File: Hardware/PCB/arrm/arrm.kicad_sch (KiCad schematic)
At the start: 9 parts, among them J1 3_pin_Molex_header, J2 3_pin_Molex_connector, J3 2_pin_Molex_header, J4 2_pin_Molex_connector, J5 2_pin_Molex_header, J6 2_pin_Molex_connector

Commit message: Rename project, cleanup
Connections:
- net Main PCB/CARRLVL_CW renamed Main PCB/CARRLVL_WIP
- net Main PCB/SIGLVL_CW renamed Main PCB/SIGLVL_WIP
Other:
- sheet Main PCB ports: added CARRLVL_WIP, SIGLVL_WIP; removed CARRLVL_CW, SIGLVL_CW
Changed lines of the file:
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@@
       (effects (font (size 1.27 1.27)) (justify right))
     )
-    (pin "SIGLVL_CW" output (at 113.03 106.68 0)
+    (pin "SIGLVL_WIP" output (at 113.03 106.68 0)
       (effects (font (size 1.27 1.27)) (justify right))
     )
@@
       (effects (font (size 1.27 1.27)) (justify right))
     )
-    (pin "CARRLVL_CW" output (at 113.03 97.79 0)
+    (pin "CARRLVL_WIP" output (at 113.03 97.79 0)
       (effects (font (size 1.27 1.27)) (justify right))
     )

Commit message: Final pre fab tweaks, Gerbers
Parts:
- J1: value 3_pin_Molex_header -> (none); footprint ao_tht:Molex_KK-254_AE-6410-03A_1x03_P2.54mm_Vertical -> (none)
- J2: renamed from J3; value 2_pin_Molex_header -> (none); footprint ao_tht:Molex_KK-254_AE-6410-02A_1x02_P2.54mm_Vertical -> (none)
- J3: renamed from J5; value 2_pin_Molex_header -> (none); footprint ao_tht:Molex_KK-254_AE-6410-02A_1x02_P2.54mm_Vertical -> (none)
- J4: renamed from J2; value 3_pin_Molex_connector -> (none)
- J5: renamed from J4; value 2_pin_Molex_connector -> (none)
- J6: value 2_pin_Molex_connector -> (none)
- RV1: value 100k -> (none); footprint ao_tht:Potentiometer_Alpha_16mm_Single_Vertical -> (none)
- RV2: renamed from RV3; value 100k -> (none); footprint ao_tht:Potentiometer_Alpha_16mm_Single_Vertical -> (none)
- RV3: renamed from RV5; value 100k -> (none); footprint ao_tht:Potentiometer_Alpha_16mm_Single_Vertical -> (none)

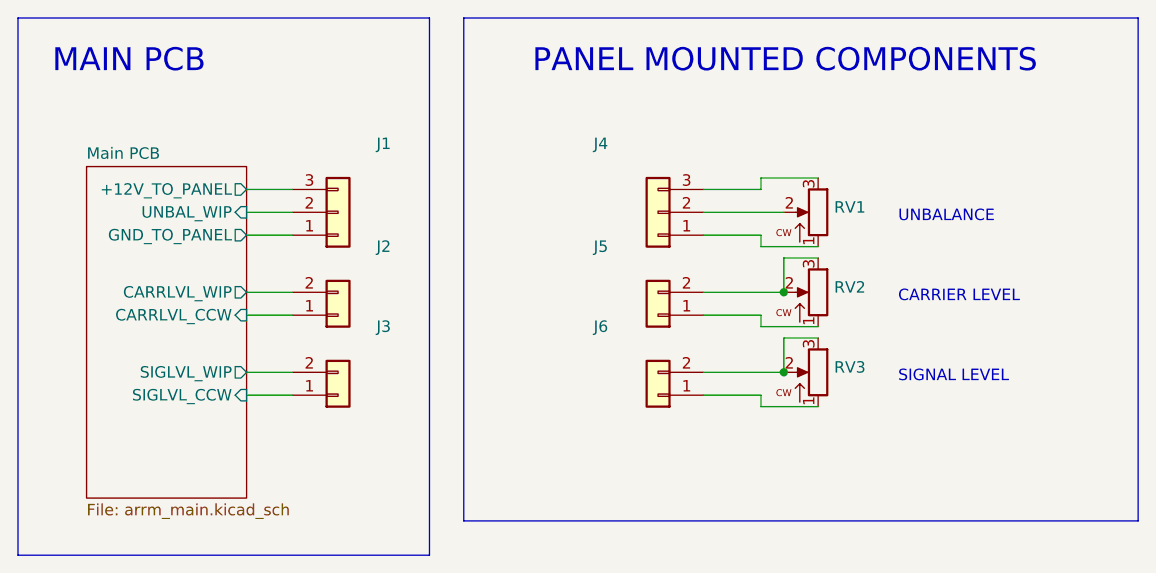
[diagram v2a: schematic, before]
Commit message: Fix footprint path; fix transformer footprint
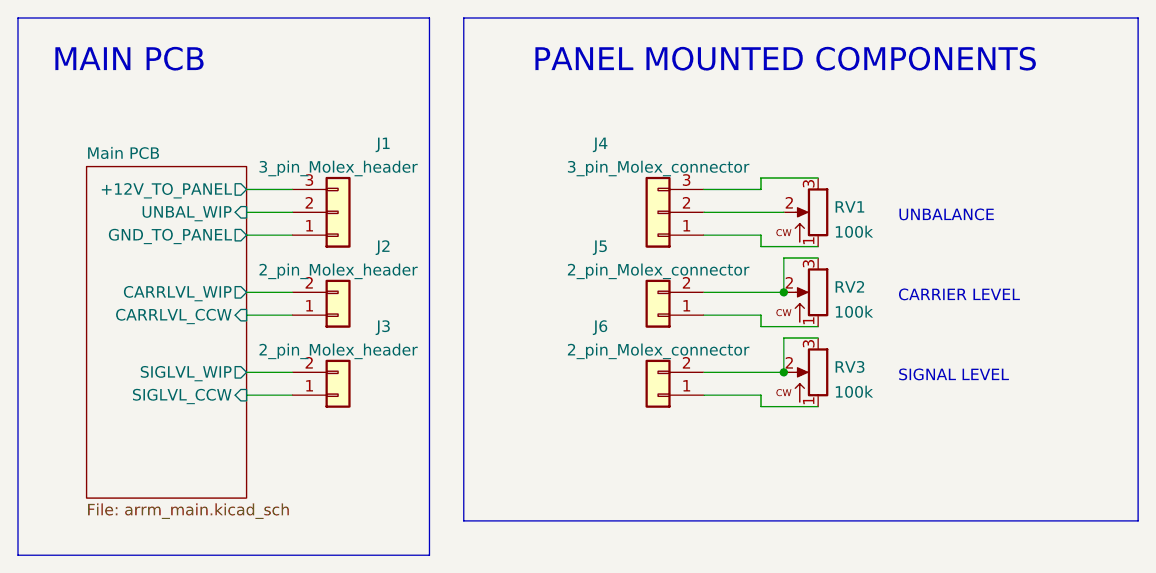
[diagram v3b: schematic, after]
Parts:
- J1: value (none) -> 3_pin_Molex_header; footprint (none) -> ao_tht:Molex_KK-254_AE-6410-03A_1x03_P2.54mm_Vertical
- J2, J3: value (none) -> 2_pin_Molex_header; footprint (none) -> ao_tht:Molex_KK-254_AE-6410-02A_1x02_P2.54mm_Vertical
- J4: value (none) -> 3_pin_Molex_connector
- J5, J6: value (none) -> 2_pin_Molex_connector
- RV1, RV2, RV3: value (none) -> 100k; footprint (none) -> ao_tht:Potentiometer_Alpha_16mm_Single_Vertical
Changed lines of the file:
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@@
       (effects (font (size 1.27 1.27)) (justify right))
     )
-    (property "Value" "" (id 1) (at 178.308 108.9022 0)
+    (property "Value" "100k" (id 1) (at 178.308 108.9022 0)
       (effects (font (size 1.27 1.27)) (justify right))
     )
-    (property "Footprint" "" (id 2) (at 176.53 106.68 0)
+    (property "Footprint" "ao_tht:Potentiometer_Alpha_16mm_Single_Vertical" (id 2) (at 176.53 106.68 0)
       (effects (font (size 1.27 1.27)) hide)
     )
@@
     (in_bom yes) (on_board no)
     (property "Reference" "J4" (id 0) (at 152.4 81.28 0))
-    (property "Value" "" (id 1) (at 158.75 83.8986 0))
+    (property "Value" "3_pin_Molex_connector" (id 1) (at 158.75 83.8986 0))
     (property "Footprint" "" (id 2) (at 158.75 88.9 0)
       (effects (font (size 1.27 1.27)) hide)
@@
       (effects (font (size 1.27 1.27)) (justify right))
     )
-    (property "Value" "" (id 1) (at 178.308 100.0122 0)
+    (property "Value" "100k" (id 1) (at 178.308 100.0122 0)
       (effects (font (size 1.27 1.27)) (justify right))
     )
-    (property "Footprint" "" (id 2) (at 176.53 97.79 0)
+    (property "Footprint" "ao_tht:Potentiometer_Alpha_16mm_Single_Vertical" (id 2) (at 176.53 97.79 0)
       (effects (font (size 1.27 1.27)) hide)
     )
@@
     (in_bom yes) (on_board yes)
     (property "Reference" "J2" (id 0) (at 128.27 92.71 0))
-    (property "Value" "" (id 1) (at 123.19 95.3286 0))
-    (property "Footprint" "" (id 2) (at 123.19 100.33 0)
+    (property "Value" "2_pin_Molex_header" (id 1) (at 123.19 95.3286 0))
+    (property "Footprint" "ao_tht:Molex_KK-254_AE-6410-02A_1x02_P2.54mm_Vertical" (id 2) (at 123.19 100.33 0)
       (effects (font (size 1.27 1.27)) hide)
     )
@@
       (effects (font (size 1.27 1.27)) (justify right))
     )
-    (property "Value" "" (id 1) (at 178.308 91.1222 0)
+    (property "Value" "100k" (id 1) (at 178.308 91.1222 0)
       (effects (font (size 1.27 1.27)) (justify right))
     )
-    (property "Footprint" "" (id 2) (at 176.53 88.9 0)
+    (property "Footprint" "ao_tht:Potentiometer_Alpha_16mm_Single_Vertical" (id 2) (at 176.53 88.9 0)
       (effects (font (size 1.27 1.27)) hide)
     )
@@
     (in_bom yes) (on_board yes)
     (property "Reference" "J1" (id 0) (at 128.27 81.28 0))
-    (property "Value" "" (id 1) (at 123.19 83.8986 0))
-    (property "Footprint" "" (id 2) (at 123.19 88.9 0)
+    (property "Value" "3_pin_Molex_header" (id 1) (at 123.19 83.8986 0))
+    (property "Footprint" "ao_tht:Molex_KK-254_AE-6410-03A_1x03_P2.54mm_Vertical" (id 2) (at 123.19 88.9 0)
       (effects (font (size 1.27 1.27)) hide)
     )
@@
     (in_bom yes) (on_board no)
     (property "Reference" "J6" (id 0) (at 152.4 101.6 0))
-    (property "Value" "" (id 1) (at 158.75 104.2186 0))
+    (property "Value" "2_pin_Molex_connector" (id 1) (at 158.75 104.2186 0))
     (property "Footprint" "" (id 2) (at 158.75 109.22 0)
       (effects (font (size 1.27 1.27)) hide)
@@
     (in_bom yes) (on_board yes)
     (property "Reference" "J3" (id 0) (at 128.27 101.6 0))
-    (property "Value" "" (id 1) (at 123.19 104.2186 0))
-    (property "Footprint" "" (id 2) (at 123.19 109.22 0)
+    (property "Value" "2_pin_Molex_header" (id 1) (at 123.19 104.2186 0))
+    (property "Footprint" "ao_tht:Molex_KK-254_AE-6410-02A_1x02_P2.54mm_Vertical" (id 2) (at 123.19 109.22 0)
       (effects (font (size 1.27 1.27)) hide)
     )
@@
     (in_bom yes) (on_board no)
     (property "Reference" "J5" (id 0) (at 152.4 92.71 0))
-    (property "Value" "" (id 1) (at 158.75 95.3286 0))
+    (property "Value" "2_pin_Molex_connector" (id 1) (at 158.75 95.3286 0))
     (property "Footprint" "" (id 2) (at 158.75 100.33 0)
       (effects (font (size 1.27 1.27)) hide)

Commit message: Post fab updates
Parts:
- J1: value 3_pin_Molex_header -> (none); footprint ao_tht:Molex_KK-254_AE-6410-03A_1x03_P2.54mm_Vertical -> (none)
- J2, J3: value 2_pin_Molex_header -> (none); footprint ao_tht:Molex_KK-254_AE-6410-02A_1x02_P2.54mm_Vertical -> (none)
- J4: value 3_pin_Molex_connector -> (none)
- J5, J6: value 2_pin_Molex_connector -> (none)
- RV1, RV2, RV3: value 100k -> (none); footprint ao_tht:Potentiometer_Alpha_16mm_Single_Vertical -> (none)
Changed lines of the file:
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@@
       (effects (font (size 1.27 1.27)) (justify right))
     )
-    (property "Value" "100k" (id 1) (at 178.308 108.9022 0)
+    (property "Value" "" (id 1) (at 178.308 108.9022 0)
       (effects (font (size 1.27 1.27)) (justify right))
     )
-    (property "Footprint" "ao_tht:Potentiometer_Alpha_16mm_Single_Vertical" (id 2) (at 176.53 106.68 0)
+    (property "Footprint" "" (id 2) (at 176.53 106.68 0)
       (effects (font (size 1.27 1.27)) hide)
     )
@@
     )
     (property "Vendor" "Tayda" (id 4) (at 176.53 106.68 0)
+      (effects (font (size 1.27 1.27)) hide)
+    )
+    (property "Description" "Linear potentiometer, panel mount" (id 5) (at 176.53 106.68 0)
       (effects (font (size 1.27 1.27)) hide)
     )
@@
     (in_bom yes) (on_board no)
     (property "Reference" "J4" (id 0) (at 152.4 81.28 0))
-    (property "Value" "3_pin_Molex_connector" (id 1) (at 158.75 83.8986 0))
+    (property "Value" "" (id 1) (at 158.75 83.8986 0))
     (property "Footprint" "" (id 2) (at 158.75 88.9 0)
       (effects (font (size 1.27 1.27)) hide)
@@
       (effects (font (size 1.27 1.27)) (justify right))
     )
-    (property "Value" "100k" (id 1) (at 178.308 100.0122 0)
+    (property "Value" "" (id 1) (at 178.308 100.0122 0)
       (effects (font (size 1.27 1.27)) (justify right))
     )
-    (property "Footprint" "ao_tht:Potentiometer_Alpha_16mm_Single_Vertical" (id 2) (at 176.53 97.79 0)
+    (property "Footprint" "" (id 2) (at 176.53 97.79 0)
       (effects (font (size 1.27 1.27)) hide)
     )
@@
     )
     (property "Vendor" "Tayda" (id 4) (at 176.53 97.79 0)
+      (effects (font (size 1.27 1.27)) hide)
+    )
+    (property "Description" "Linear potentiometer, panel mount" (id 5) (at 176.53 97.79 0)
       (effects (font (size 1.27 1.27)) hide)
     )
@@
     (in_bom yes) (on_board yes)
     (property "Reference" "J2" (id 0) (at 128.27 92.71 0))
-    (property "Value" "2_pin_Molex_header" (id 1) (at 123.19 95.3286 0))
-    (property "Footprint" "ao_tht:Molex_KK-254_AE-6410-02A_1x02_P2.54mm_Vertical" (id 2) (at 123.19 100.33 0)
+    (property "Value" "" (id 1) (at 123.19 95.3286 0))
+    (property "Footprint" "" (id 2) (at 123.19 100.33 0)
       (effects (font (size 1.27 1.27)) hide)
     )
@@
       (effects (font (size 1.27 1.27)) (justify right))
     )
-    (property "Value" "100k" (id 1) (at 178.308 91.1222 0)
+    (property "Value" "" (id 1) (at 178.308 91.1222 0)
       (effects (font (size 1.27 1.27)) (justify right))
     )
-    (property "Footprint" "ao_tht:Potentiometer_Alpha_16mm_Single_Vertical" (id 2) (at 176.53 88.9 0)
+    (property "Footprint" "" (id 2) (at 176.53 88.9 0)
       (effects (font (size 1.27 1.27)) hide)
     )
@@
     )
     (property "Vendor" "Tayda" (id 4) (at 176.53 88.9 0)
+      (effects (font (size 1.27 1.27)) hide)
+    )
+    (property "Description" "Linear potentiometer, panel mount" (id 5) (at 176.53 88.9 0)
       (effects (font (size 1.27 1.27)) hide)
     )
@@
     (in_bom yes) (on_board yes)
     (property "Reference" "J1" (id 0) (at 128.27 81.28 0))
-    (property "Value" "3_pin_Molex_header" (id 1) (at 123.19 83.8986 0))
-    (property "Footprint" "ao_tht:Molex_KK-254_AE-6410-03A_1x03_P2.54mm_Vertical" (id 2) (at 123.19 88.9 0)
+    (property "Value" "" (id 1) (at 123.19 83.8986 0))
+    (property "Footprint" "" (id 2) (at 123.19 88.9 0)
       (effects (font (size 1.27 1.27)) hide)
     )
@@
     (in_bom yes) (on_board no)
     (property "Reference" "J6" (id 0) (at 152.4 101.6 0))
-    (property "Value" "2_pin_Molex_connector" (id 1) (at 158.75 104.2186 0))
+    (property "Value" "" (id 1) (at 158.75 104.2186 0))
     (property "Footprint" "" (id 2) (at 158.75 109.22 0)
       (effects (font (size 1.27 1.27)) hide)
@@
     (in_bom yes) (on_board yes)
     (property "Reference" "J3" (id 0) (at 128.27 101.6 0))
-    (property "Value" "2_pin_Molex_header" (id 1) (at 123.19 104.2186 0))
-    (property "Footprint" "ao_tht:Molex_KK-254_AE-6410-02A_1x02_P2.54mm_Vertical" (id 2) (at 123.19 109.22 0)
+    (property "Value" "" (id 1) (at 123.19 104.2186 0))
+    (property "Footprint" "" (id 2) (at 123.19 109.22 0)
       (effects (font (size 1.27 1.27)) hide)
     )
@@
     (in_bom yes) (on_board no)
     (property "Reference" "J5" (id 0) (at 152.4 92.71 0))
-    (property "Value" "2_pin_Molex_connector" (id 1) (at 158.75 95.3286 0))
+    (property "Value" "" (id 1) (at 158.75 95.3286 0))
     (property "Footprint" "" (id 2) (at 158.75 100.33 0)
       (effects (font (size 1.27 1.27)) hide)

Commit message: Docs, pics, new Gerbers
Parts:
- RV1, RV2, RV3: SKU (none) -> A-1984
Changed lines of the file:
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@@
+      (effects (font (size 1.27 1.27)) hide)
+    )
+    (property "SKU" "A-1984" (id 6) (at 176.53 106.68 0)
       (effects (font (size 1.27 1.27)) hide)
     )
@@
       (effects (font (size 1.27 1.27)) hide)
     )
+    (property "SKU" "A-1984" (id 6) (at 176.53 97.79 0)
+      (effects (font (size 1.27 1.27)) hide)
+    )
     (pin "1")
     (pin "2")
@@
       (effects (font (size 1.27 1.27)) hide)
     )
+    (property "SKU" "A-1984" (id 6) (at 176.53 88.9 0)
+      (effects (font (size 1.27 1.27)) hide)
+    )

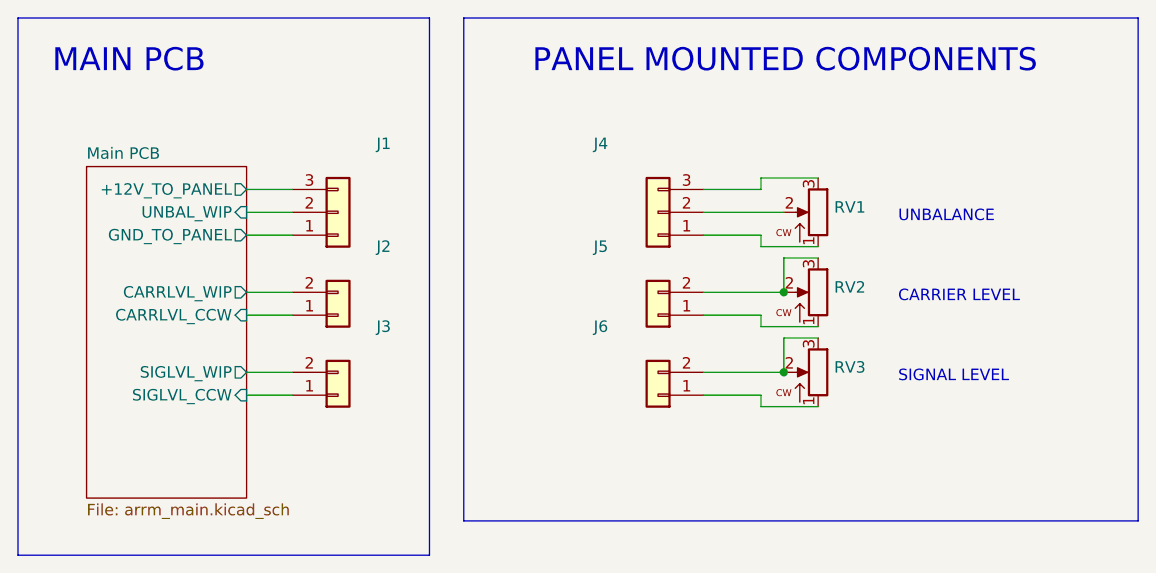
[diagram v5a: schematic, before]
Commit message: R4 should be 330k
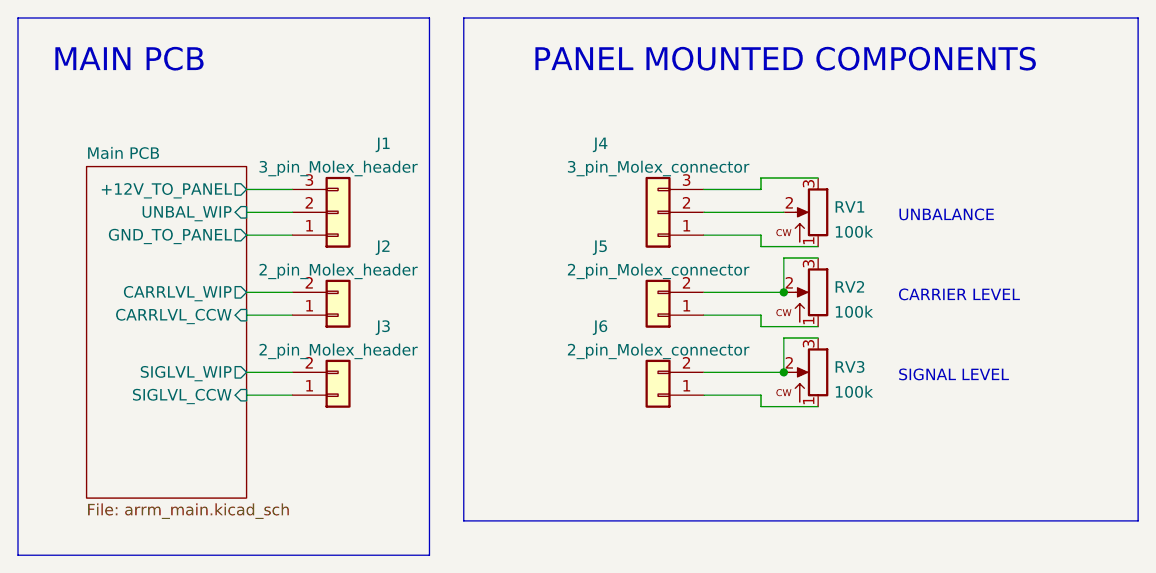
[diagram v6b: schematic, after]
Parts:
- J1: value (none) -> 3_pin_Molex_header; footprint (none) -> ao_tht:Molex_KK-254_AE-6410-03A_1x03_P2.54mm_Vertical
- J2, J3: value (none) -> 2_pin_Molex_header; footprint (none) -> ao_tht:Molex_KK-254_AE-6410-02A_1x02_P2.54mm_Vertical
- J4: value (none) -> 3_pin_Molex_connector
- J5, J6: value (none) -> 2_pin_Molex_connector
- RV1, RV2, RV3: value (none) -> 100k; footprint (none) -> ao_tht:Potentiometer_Alpha_16mm_Single_Vertical
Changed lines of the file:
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@@
       (effects (font (size 1.27 1.27)) (justify right))
     )
-    (property "Value" "" (id 1) (at 178.308 108.9022 0)
-      (effects (font (size 1.27 1.27)) (justify right))
-    )
-    (property "Footprint" "" (id 2) (at 176.53 106.68 0)
+    (property "Value" "100k" (id 1) (at 178.308 108.9022 0)
+      (effects (font (size 1.27 1.27)) (justify right))
+    )
+    (property "Footprint" "ao_tht:Potentiometer_Alpha_16mm_Single_Vertical" (id 2) (at 176.53 106.68 0)
       (effects (font (size 1.27 1.27)) hide)
     )
@@
     (in_bom yes) (on_board no)
     (property "Reference" "J4" (id 0) (at 152.4 81.28 0))
-    (property "Value" "" (id 1) (at 158.75 83.8986 0))
+    (property "Value" "3_pin_Molex_connector" (id 1) (at 158.75 83.8986 0))
     (property "Footprint" "" (id 2) (at 158.75 88.9 0)
       (effects (font (size 1.27 1.27)) hide)
@@
       (effects (font (size 1.27 1.27)) (justify right))
     )
-    (property "Value" "" (id 1) (at 178.308 100.0122 0)
-      (effects (font (size 1.27 1.27)) (justify right))
-    )
-    (property "Footprint" "" (id 2) (at 176.53 97.79 0)
+    (property "Value" "100k" (id 1) (at 178.308 100.0122 0)
+      (effects (font (size 1.27 1.27)) (justify right))
+    )
+    (property "Footprint" "ao_tht:Potentiometer_Alpha_16mm_Single_Vertical" (id 2) (at 176.53 97.79 0)
       (effects (font (size 1.27 1.27)) hide)
     )
@@
     (in_bom yes) (on_board yes)
     (property "Reference" "J2" (id 0) (at 128.27 92.71 0))
-    (property "Value" "" (id 1) (at 123.19 95.3286 0))
-    (property "Footprint" "" (id 2) (at 123.19 100.33 0)
+    (property "Value" "2_pin_Molex_header" (id 1) (at 123.19 95.3286 0))
+    (property "Footprint" "ao_tht:Molex_KK-254_AE-6410-02A_1x02_P2.54mm_Vertical" (id 2) (at 123.19 100.33 0)
       (effects (font (size 1.27 1.27)) hide)
     )
@@
       (effects (font (size 1.27 1.27)) (justify right))
     )
-    (property "Value" "" (id 1) (at 178.308 91.1222 0)
-      (effects (font (size 1.27 1.27)) (justify right))
-    )
-    (property "Footprint" "" (id 2) (at 176.53 88.9 0)
+    (property "Value" "100k" (id 1) (at 178.308 91.1222 0)
+      (effects (font (size 1.27 1.27)) (justify right))
+    )
+    (property "Footprint" "ao_tht:Potentiometer_Alpha_16mm_Single_Vertical" (id 2) (at 176.53 88.9 0)
       (effects (font (size 1.27 1.27)) hide)
     )
@@
     (in_bom yes) (on_board yes)
     (property "Reference" "J1" (id 0) (at 128.27 81.28 0))
-    (property "Value" "" (id 1) (at 123.19 83.8986 0))
-    (property "Footprint" "" (id 2) (at 123.19 88.9 0)
+    (property "Value" "3_pin_Molex_header" (id 1) (at 123.19 83.8986 0))
+    (property "Footprint" "ao_tht:Molex_KK-254_AE-6410-03A_1x03_P2.54mm_Vertical" (id 2) (at 123.19 88.9 0)
       (effects (font (size 1.27 1.27)) hide)
     )
@@
     (in_bom yes) (on_board no)
     (property "Reference" "J6" (id 0) (at 152.4 101.6 0))
-    (property "Value" "" (id 1) (at 158.75 104.2186 0))
+    (property "Value" "2_pin_Molex_connector" (id 1) (at 158.75 104.2186 0))
     (property "Footprint" "" (id 2) (at 158.75 109.22 0)
       (effects (font (size 1.27 1.27)) hide)
@@
     (in_bom yes) (on_board yes)
     (property "Reference" "J3" (id 0) (at 128.27 101.6 0))
-    (property "Value" "" (id 1) (at 123.19 104.2186 0))
-    (property "Footprint" "" (id 2) (at 123.19 109.22 0)
+    (property "Value" "2_pin_Molex_header" (id 1) (at 123.19 104.2186 0))
+    (property "Footprint" "ao_tht:Molex_KK-254_AE-6410-02A_1x02_P2.54mm_Vertical" (id 2) (at 123.19 109.22 0)
       (effects (font (size 1.27 1.27)) hide)
     )
@@
     (in_bom yes) (on_board no)
     (property "Reference" "J5" (id 0) (at 152.4 92.71 0))
-    (property "Value" "" (id 1) (at 158.75 95.3286 0))
+    (property "Value" "2_pin_Molex_connector" (id 1) (at 158.75 95.3286 0))
     (property "Footprint" "" (id 2) (at 158.75 100.33 0)
       (effects (font (size 1.27 1.27)) hide)
@@
     )
     (path "/a461a421-5a27-42b0-84e6-0ecc9405c34f/f4c60067-3d1d-40b1-bfde-67834e6237d4"
-      (reference "R4") (unit 1) (value "330R") (footprint "ao_tht:R_Axial_DIN0207_L6.3mm_D2.5mm_P10.16mm_Horizontal")
+      (reference "R4") (unit 1) (value "330k") (footprint "ao_tht:R_Axial_DIN0207_L6.3mm_D2.5mm_P10.16mm_Horizontal")
     )
     (path "/a461a421-5a27-42b0-84e6-0ecc9405c34f/6707a543-3cd8-4d3a-b815-e9762accce1f"
